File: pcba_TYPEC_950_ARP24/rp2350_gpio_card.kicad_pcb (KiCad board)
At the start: 4 copper layers, 26 x 30 mm, 37 parts, among them J1 Conn_01x10_Pin, J2 Conn_01x10_Pin, P1 USB_C_Plug_USB2.0, U1 RP2350_60QFN, U2 W25Q128JVS, U4 AP2127K-3.3, Y1 ABM8-272-T3

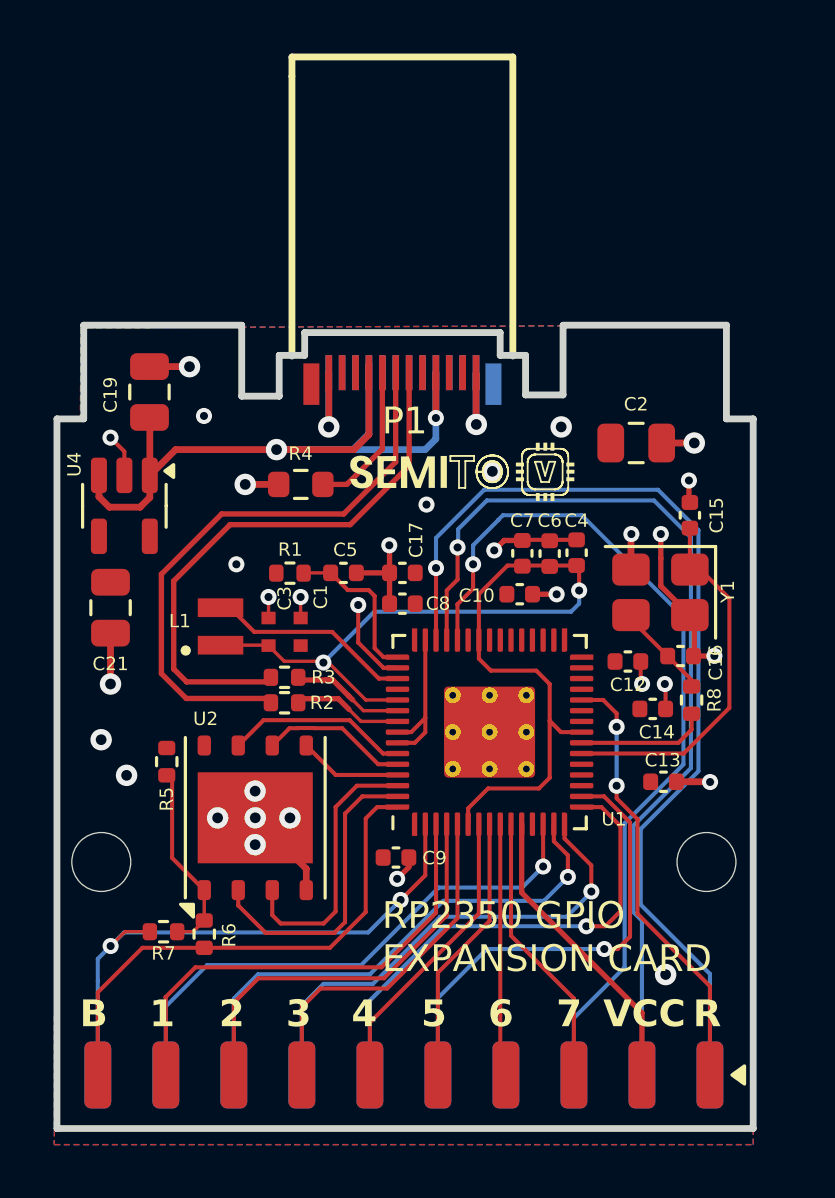
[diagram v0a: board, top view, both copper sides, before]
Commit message: minor type-c fix
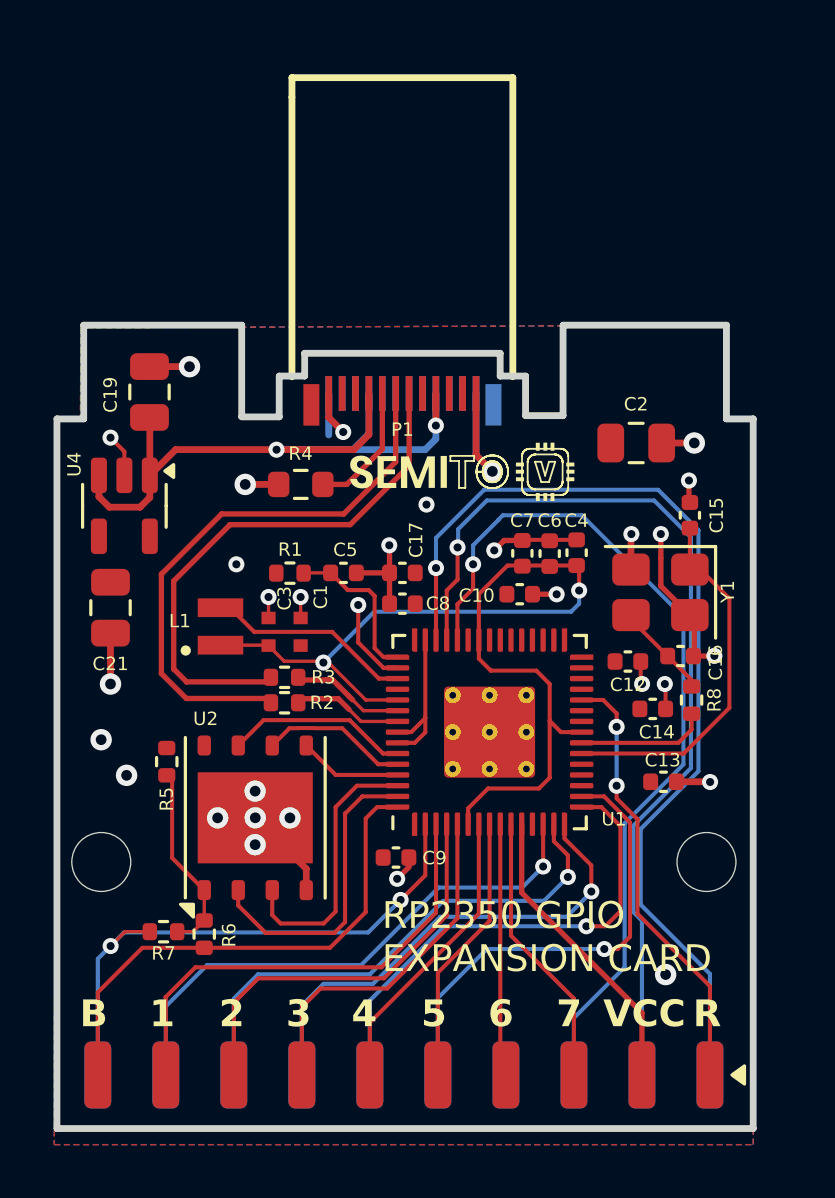
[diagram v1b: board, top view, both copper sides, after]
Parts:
- moved P1 0.77 mm to (103.5, 54.4)
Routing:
- net VBUS: track 31.2 -> 27.7 mm
- net GND: track 45.4 -> 46.9 mm, vias 34 -> 31
- net Net-(P1-CC): track 5.93 -> 4.84 mm
- net /USB_D-: track 21.6 -> 20.5 mm
- net /USB_D+: track 22.4 -> 21.3 mm
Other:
- outline, holes or cut-outs redrawn
